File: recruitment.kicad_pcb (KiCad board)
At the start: 2 copper layers, 0 parts

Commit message: place footprints
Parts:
- added C201: 10µF 50V, Capacitor_SMD:C_1210_3225Metric, F.Cu at (64.0, 89.0)
- added C202: 100nF 50V, Capacitor_SMD:C_0603_1608Metric, F.Cu at (69.3, 91.0)
- added C203: 1µF 50V, Capacitor_SMD:C_0805_2012Metric, F.Cu at (56.6, 77.7)
- added C204: 10µF 16V, Capacitor_SMD:C_0805_2012Metric, F.Cu at (56.6, 82.3)
- added C205: 100nF 16V, Capacitor_SMD:C_0603_1608Metric, F.Cu at (56.6, 87.0)
- added C401: 100nF 16V, Capacitor_SMD:C_0603_1608Metric, B.Cu at (128.6, 70.4)
- added C402: 15nF 50V C0G, Capacitor_SMD:C_0603_1608Metric, F.Cu at (124.4, 77.1)
- added C501: 100nF 16V, Capacitor_SMD:C_0603_1608Metric, F.Cu at (135.3, 77.6)
- added C502: 100nF 16V, Capacitor_SMD:C_0603_1608Metric, F.Cu at (141.2, 85.6)
- added C503: 100nF 16V, Capacitor_SMD:C_0603_1608Metric, F.Cu at (140.9, 89.5)
- added D201: SMBJ18CA, Diode_SMD:D_SMB, F.Cu at (69.9, 104.0)
- added D202: 12V, Diode_SMD:D_SOD-123, F.Cu at (65.5, 94.6)
- added D203: PWR yellow-green, LED_SMD:LED_0603_1608Metric, F.Cu at (112.0, 114.0)
- added D301: 1N4148W, Diode_SMD:D_SOD-123, F.Cu at (93.1, 94.0)
- added D302: 18V 1W, Diode_SMD:D_SMA, F.Cu at (86.0, 94.0)
- added D501: TRIP red, LED_SMD:LED_0603_1608Metric, F.Cu at (120.5, 114.0)
- added D502: RELAY yellow, LED_SMD:LED_0603_1608Metric, F.Cu at (116.5, 114.0)
- added F201: 0.5A 30V, Fuse:Fuse_1812_4532Metric, F.Cu at (63.0, 104.0)
- added H101: MountingHole, MountingHole:MountingHole_3.2mm_M3, F.Cu at (54.0, 54.0)
- added H102: MountingHole, MountingHole:MountingHole_3.2mm_M3, F.Cu at (146.0, 54.0)
- added H103: MountingHole, MountingHole:MountingHole_3.2mm_M3, F.Cu at (54.0, 116.0)
- added H104: MountingHole, MountingHole:MountingHole_3.2mm_M3, F.Cu at (146.0, 116.0)
- added J201: Micro-Fit 2P, Connector_Molex:Molex_Micro-Fit_3.0_43650-0215_1x02_P3.00mm_Vertical, F.Cu at (56.0, 104.0)
- added J301: LOAD_IN, MountingHole:MountingHole_4.3mm_M4_Pad, F.Cu at (64.0, 62.0)
- added J302: LOAD_OUT, MountingHole:MountingHole_4.3mm_M4_Pad, F.Cu at (138.0, 62.0)
- added K301: GE9J-1-P-E-UVD DC12, monitor:Relay_Omron_G9EJ-1-P-E, F.Cu at (90.0, 74.0)
- added Q201: Si2319CDS, Package_TO_SOT_SMD:SOT-23, F.Cu at (65.5, 98.5)
- added Q301: BCP56-16, Package_TO_SOT_SMD:SOT-223, F.Cu at (100.5, 99.0)
- added Q302: BC847B, Package_TO_SOT_SMD:SOT-23, F.Cu at (96.5, 106.6)
- added R201: 100k, Resistor_SMD:R_0603_1608Metric, F.Cu at (70.6, 97.6)
- added R202: 1k, Resistor_SMD:R_0603_1608Metric, F.Cu at (112.0, 110.6)
- added R301: 8.2R, Resistor_SMD:R_0805_2012Metric, F.Cu at (102.3, 106.0)
- added R302: 820R, Resistor_SMD:R_0603_1608Metric, F.Cu at (92.6, 101.5)
- added R303: 10k, Resistor_SMD:R_0603_1608Metric, F.Cu at (92.6, 103.4)
- added R304: 1k, Resistor_SMD:R_0603_1608Metric, F.Cu at (100.3, 110.0)
- added R401: 100k, Resistor_SMD:R_0603_1608Metric, F.Cu at (122.2, 73.2)
- added R402: 10k, Resistor_SMD:R_0603_1608Metric, F.Cu at (125.4, 73.2)
- added R403: 1k, Resistor_SMD:R_0603_1608Metric, F.Cu at (122.1, 80.1)
- added R501: 37.4k, Resistor_SMD:R_0603_1608Metric, F.Cu at (126.6, 82.6)
- added R502: 27.4k, Resistor_SMD:R_0603_1608Metric, F.Cu at (129.8, 82.6)
- added R503: 22.1k, Resistor_SMD:R_0603_1608Metric, F.Cu at (133.0, 82.6)
- added R504: 10k, Resistor_SMD:R_0603_1608Metric, F.Cu at (133.3, 86.9)
- added R505: 1k, Resistor_SMD:R_0603_1608Metric, F.Cu at (120.5, 110.6)
- added R506: 1k, Resistor_SMD:R_0603_1608Metric, F.Cu at (116.5, 110.6)
- added SW401: TEST, Button_Switch_SMD:SW_SPST_PTS645Sx43SMTR92, F.Cu at (134.0, 112.6)
- added TP201: +VIN_PROT, TestPoint:TestPoint_Pad_D1.5mm, F.Cu at (67.5, 110.5)
- added TP202: +3V3, TestPoint:TestPoint_Pad_D1.5mm, F.Cu at (73.5, 110.5)
- added TP203: GND, TestPoint:TestPoint_Keystone_5000-5004_Miniature, F.Cu at (62.0, 110.5)
- added TP301: COIL_RS, TestPoint:TestPoint_Pad_D1.5mm, F.Cu at (104.8, 110.5)
- added TP401: V_SENSE, TestPoint:TestPoint_Pad_D1.5mm, F.Cu at (118.5, 76.5)
- added TP501: Vth_Hi, TestPoint:TestPoint_Pad_D1.5mm, F.Cu at (126.6, 85.6)
- added TP502: FAULT_N, TestPoint:TestPoint_Pad_D1.5mm, F.Cu at (121.0, 90.0)
- added U201: TPS7B6933-Q1, Package_TO_SOT_SMD:SOT-223-3_TabPin2, F.Cu at (64.0, 80.0)
- added U401: ACS781LLRTR-050B-T, Sensor_Current:Allegro_PSOF-7_4.8x6.4mm_P1.60mm, B.Cu at (126.0, 65.0)
- added U501: TLV1702, Package_SO:VSSOP-8_3x3mm_P0.65mm, F.Cu at (130.0, 78.0)
- added U502: MAX809S, Package_TO_SOT_SMD:SOT-23, F.Cu at (137.4, 94.3)
- added U503: 74LVC00, Package_SO:SOIC-14_3.9x8.7mm_P1.27mm, F.Cu at (130.0, 94.5)
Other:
- board outline added: 100 x 70 mm

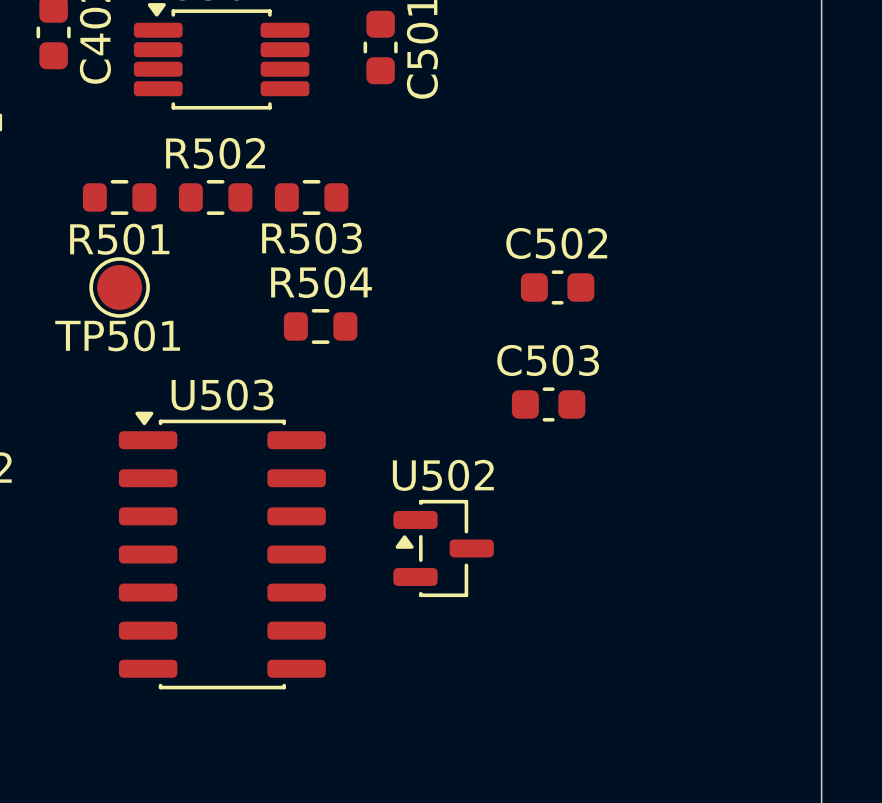
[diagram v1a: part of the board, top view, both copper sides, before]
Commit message: Add Power net class, 48V clearance rules and placement fixes
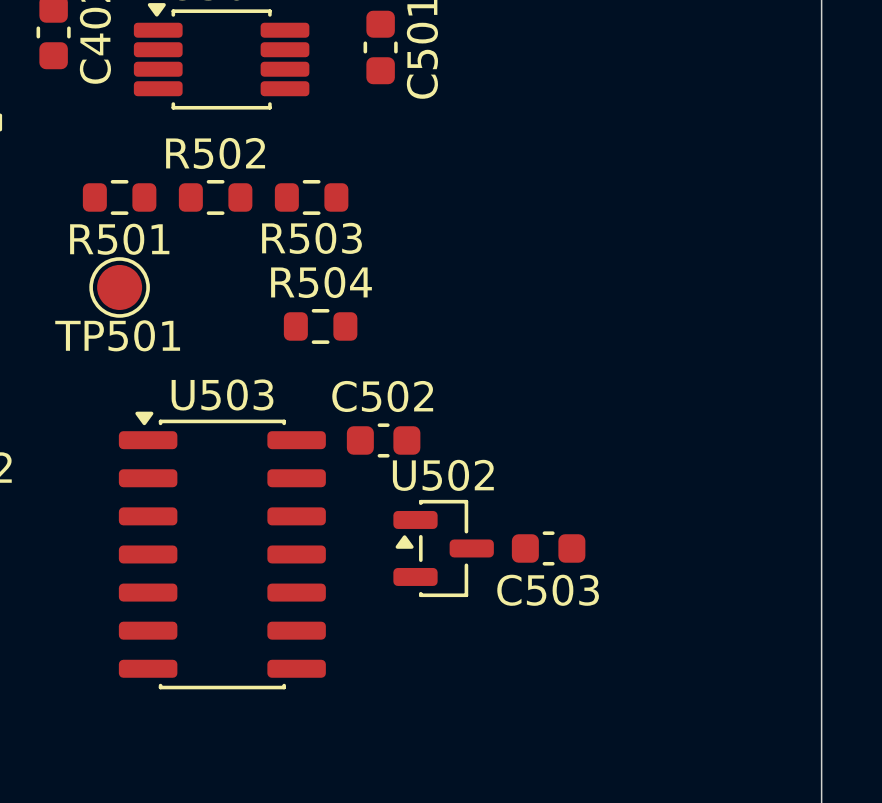
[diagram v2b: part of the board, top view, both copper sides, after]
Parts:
- K301: value GE9J-1-P-E-UVD DC12 -> G9EJ-1-P-E-UVD DC12
- moved C502 7.72 mm to (135.4, 90.7)
- moved C503 4.80 mm to (140.9, 94.3), turned to 180 degrees
- turned R503 to 180 degrees
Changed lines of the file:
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@@
 	(footprint "Capacitor_SMD:C_0603_1608Metric"
 		(layer "F.Cu")
-		(at 141.2 85.6)
+		(at 135.4 90.7)
 		(descr "Capacitor SMD 0603 (1608 Metric), square (rectangular) end terminal, IPC-7351 nominal, (Body size source: IPC-SM-782 page 76, https://www.pcb-3d.com/wordpress/wp-content/uploads/ipc-sm-782a_amendment_1_and_2.pdf)")
 		(tags "capacitor")
@@
 			)
 		)
-		(property "Value" "GE9J-1-P-E-UVD DC12"
+		(property "Value" "G9EJ-1-P-E-UVD DC12"
 			(at 0 1 270)
 			(unlocked yes)
@@
 	(footprint "Capacitor_SMD:C_0603_1608Metric"
 		(layer "F.Cu")
-		(at 140.9 89.5)
+		(at 140.9 94.3 180)
 		(descr "Capacitor SMD 0603 (1608 Metric), square (rectangular) end terminal, IPC-7351 nominal, (Body size source: IPC-SM-782 page 76, https://www.pcb-3d.com/wordpress/wp-content/uploads/ipc-sm-782a_amendment_1_and_2.pdf)")
 		(tags "capacitor")
@@
 		(duplicate_pad_numbers_are_jumpers no)
 		(fp_line
-			(start -0.14058 -0.51)
-			(end 0.14058 -0.51)
+			(start -0.14058 0.51)
+			(end 0.14058 0.51)
 			(stroke
 				(width 0.12)
@@
 		)
 		(fp_line
-			(start -0.14058 0.51)
-			(end 0.14058 0.51)
+			(start -0.14058 -0.51)
+			(end 0.14058 -0.51)
 			(stroke
 				(width 0.12)
@@
 		)
 		(pad "1" smd roundrect
-			(at -0.775 0)
+			(at -0.775 0 180)
 			(size 0.9 0.95)
 			(layers "F.Cu" "F.Mask" "F.Paste")
@@
 		)
 		(pad "2" smd roundrect
-			(at 0.775 0)
+			(at 0.775 0 180)
 			(size 0.9 0.95)
 			(layers "F.Cu" "F.Mask" "F.Paste")
@@
 	(footprint "Resistor_SMD:R_0603_1608Metric"
 		(layer "F.Cu")
-		(at 133 82.6)
+		(at 133 82.6 180)
 		(descr "Resistor SMD 0603 (1608 Metric), square (rectangular) end terminal, IPC-7351 nominal, (Body size source: IPC-SM-782 page 72, https://www.pcb-3d.com/wordpress/wp-content/uploads/ipc-sm-782a_amendment_1_and_2.pdf)")
 		(tags "resistor")
 		(property "Reference" "R503"
-			(at 0 1.4 0)
+			(at 0 -1.4 0)
 			(layer "F.SilkS")
 			(effects
@@
 		(duplicate_pad_numbers_are_jumpers no)
 		(fp_line
-			(start -0.237258 -0.5225)
-			(end 0.237258 -0.5225)
+			(start -0.237258 0.5225)
+			(end 0.237258 0.5225)
 			(stroke
 				(width 0.12)
@@
 		)
 		(fp_line
-			(start -0.237258 0.5225)
-			(end 0.237258 0.5225)
+			(start -0.237258 -0.5225)
+			(end 0.237258 -0.5225)
 			(stroke
 				(width 0.12)
@@
 		)
 		(pad "1" smd roundrect
-			(at -0.825 0)
+			(at -0.825 0 180)
 			(size 0.8 0.95)
 			(layers "F.Cu" "F.Mask" "F.Paste")
@@
 		)
 		(pad "2" smd roundrect
-			(at 0.825 0)
+			(at 0.825 0 180)
 			(size 0.8 0.95)
 			(layers "F.Cu" "F.Mask" "F.Paste")

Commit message: Route power path
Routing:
- net /Relay/LOAD_OUT: vias 0 -> 5
- net /Relay/LOAD_MID: vias 0 -> 12
- added copper zone on B.Cu, net /Relay/LOAD_IN
- added copper zone on F.Cu, net /Relay/LOAD_IN
- added copper zone on B.Cu, net /Relay/LOAD_MID
- added copper zone on F.Cu, net /Relay/LOAD_MID
- added copper zone on B.Cu, net /Relay/LOAD_OUT
- added copper zone on F.Cu, net /Relay/LOAD_OUT

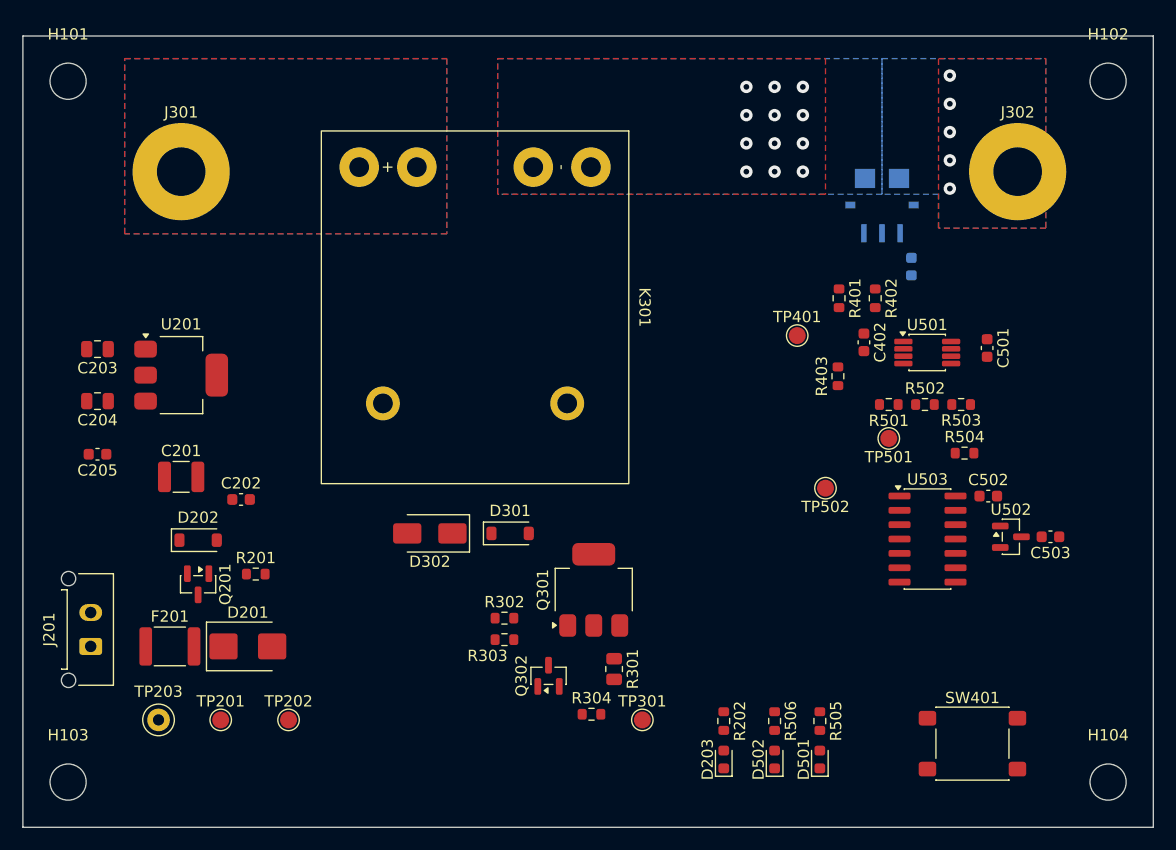
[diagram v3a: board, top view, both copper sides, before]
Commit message: Route coil driver and power supply
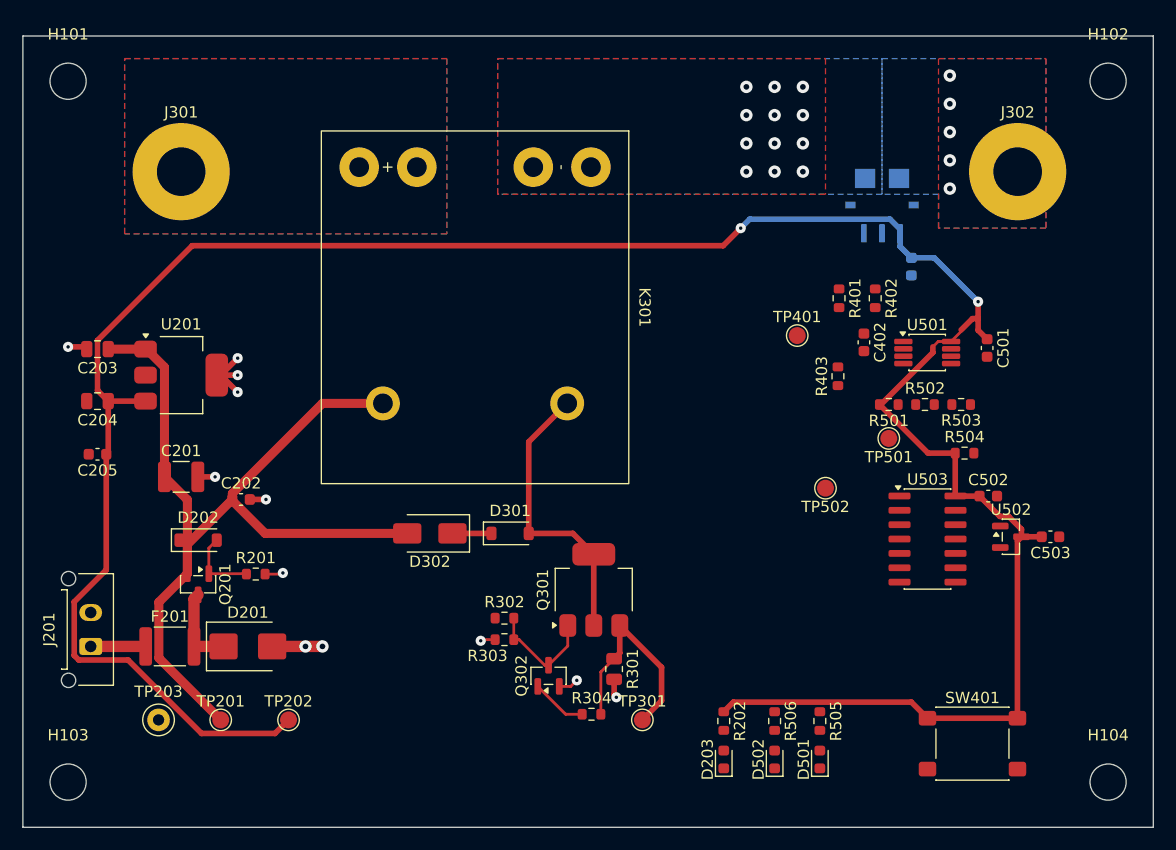
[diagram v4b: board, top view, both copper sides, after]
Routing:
- net +3V3: track 0.00 -> 222.6 mm, vias 0 -> 2
- net +VIN_PROT: track 0.00 -> 84.0 mm
- net /Relay/COIL_N: track 0.00 -> 25.7 mm
- net GND: track 0.00 -> 22.0 mm, vias 0 -> 12
- net /Relay/COIL_RS: track 0.00 -> 19.1 mm
- net /Relay/COIL_DRV: track 0.00 -> 10.1 mm
- net /Power/VIN_FUSED: track 0.00 -> 7.33 mm
- net /Power/Q201_G: track 0.00 -> 6.59 mm
- net Net-(Q302-B): track 0.00 -> 4.95 mm
- net /Power/VIN_RAW: track 0.00 -> 4.86 mm
- net Net-(D301-K): track 0.00 -> 3.45 mm

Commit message: Route sensing and trip logic
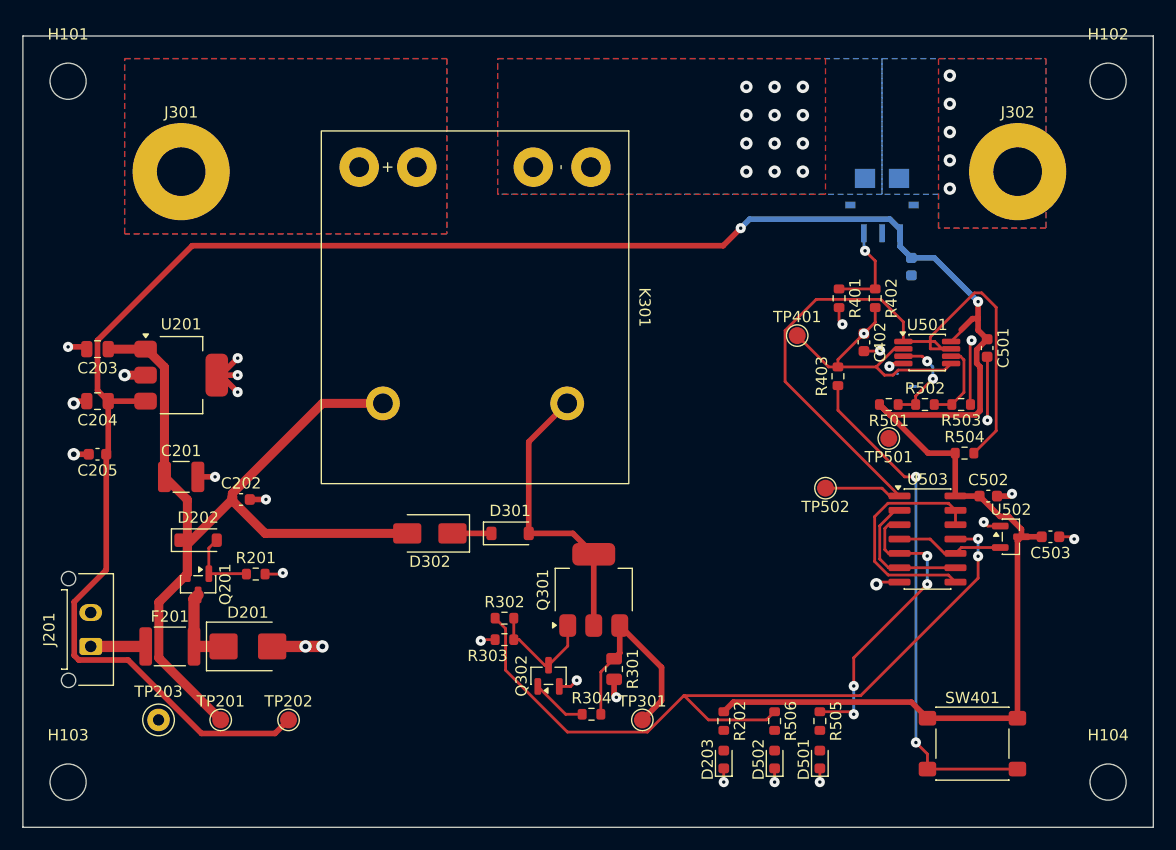
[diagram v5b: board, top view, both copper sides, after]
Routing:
- net /Relay/RELAY_EN: track 0.00 -> 69.4 mm, vias 0 -> 2
- net /Trip Logic/FAULT_N: track 0.00 -> 68.9 mm
- net Net-(R403-Pad1): track 0.00 -> 45.8 mm, vias 0 -> 2
- net GND: track 22.0 -> 52.3 mm, vias 12 -> 27
- net /Trip Logic/TRIP: track 0.00 -> 27.1 mm, vias 0 -> 4
- net /Sensing/V_SENSE: track 0.00 -> 25.7 mm, vias 0 -> 1
- net /Trip Logic/RELAY_EN_N: track 0.00 -> 21.1 mm
- net /Trip Logic/TRIP_N: track 0.00 -> 12.3 mm
- net /Trip Logic/PR_N: track 0.00 -> 9.65 mm
- net /Sensing/ACS_VOUT: track 0.00 -> 8.54 mm, vias 0 -> 1
- net /Trip Logic/Vth_Hi: track 0.00 -> 8.51 mm, vias 0 -> 2
- net +3V3: track 222.6 -> 230.1 mm
- net /Trip Logic/Vth_Lo: track 0.00 -> 7.22 mm

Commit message: Add coil copper and ground plane
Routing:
- net /Trip Logic/Vth_Hi: track 8.51 -> 15.5 mm
- net Net-(D502-A): track 0.00 -> 1.79 mm
- net Net-(D501-A): track 0.00 -> 1.79 mm
- net Net-(D203-A): track 0.00 -> 1.79 mm
- net /Sensing/V_SENSE: track 25.7 -> 25.2 mm, vias 1 -> 0
- net /Relay/COIL_N: vias 0 -> 12
- added copper zone on B.Cu, net /Relay/COIL_N
- added copper zone on F.Cu, net /Relay/COIL_N
- added copper zone on B.Cu, net GND
